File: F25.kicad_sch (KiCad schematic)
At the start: 37 parts, among them J3 B2B-PH-K-S, J4 USB_C_Receptacle_USB2.0_16P, Q1 IRLML6244, SW1 RESET, SW2 BOOT, U2 MPU-6050, U3 MS5611-01BA, U4 ESP32-S3-WROOM-1-N8, U5 AP2112K-3.3

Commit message: General Updates
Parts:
- U4: footprint ESP:ESP32-S3-WROOM-1_EXP -> RF_Module:ESP32-S3-WROOM-1
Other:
- note added: "I/O"
- note added: "MCU"
- note added: "MPU6050"
- note added: "MS5611"
- note added: "PULLUPS"
- title: Eggtimer Ion Flight Computer  -> MARS F25 Board
- moved on the sheet: C1, C10, C11, C2, C3, C4, C5, C6, C7, C8, CR1, D1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

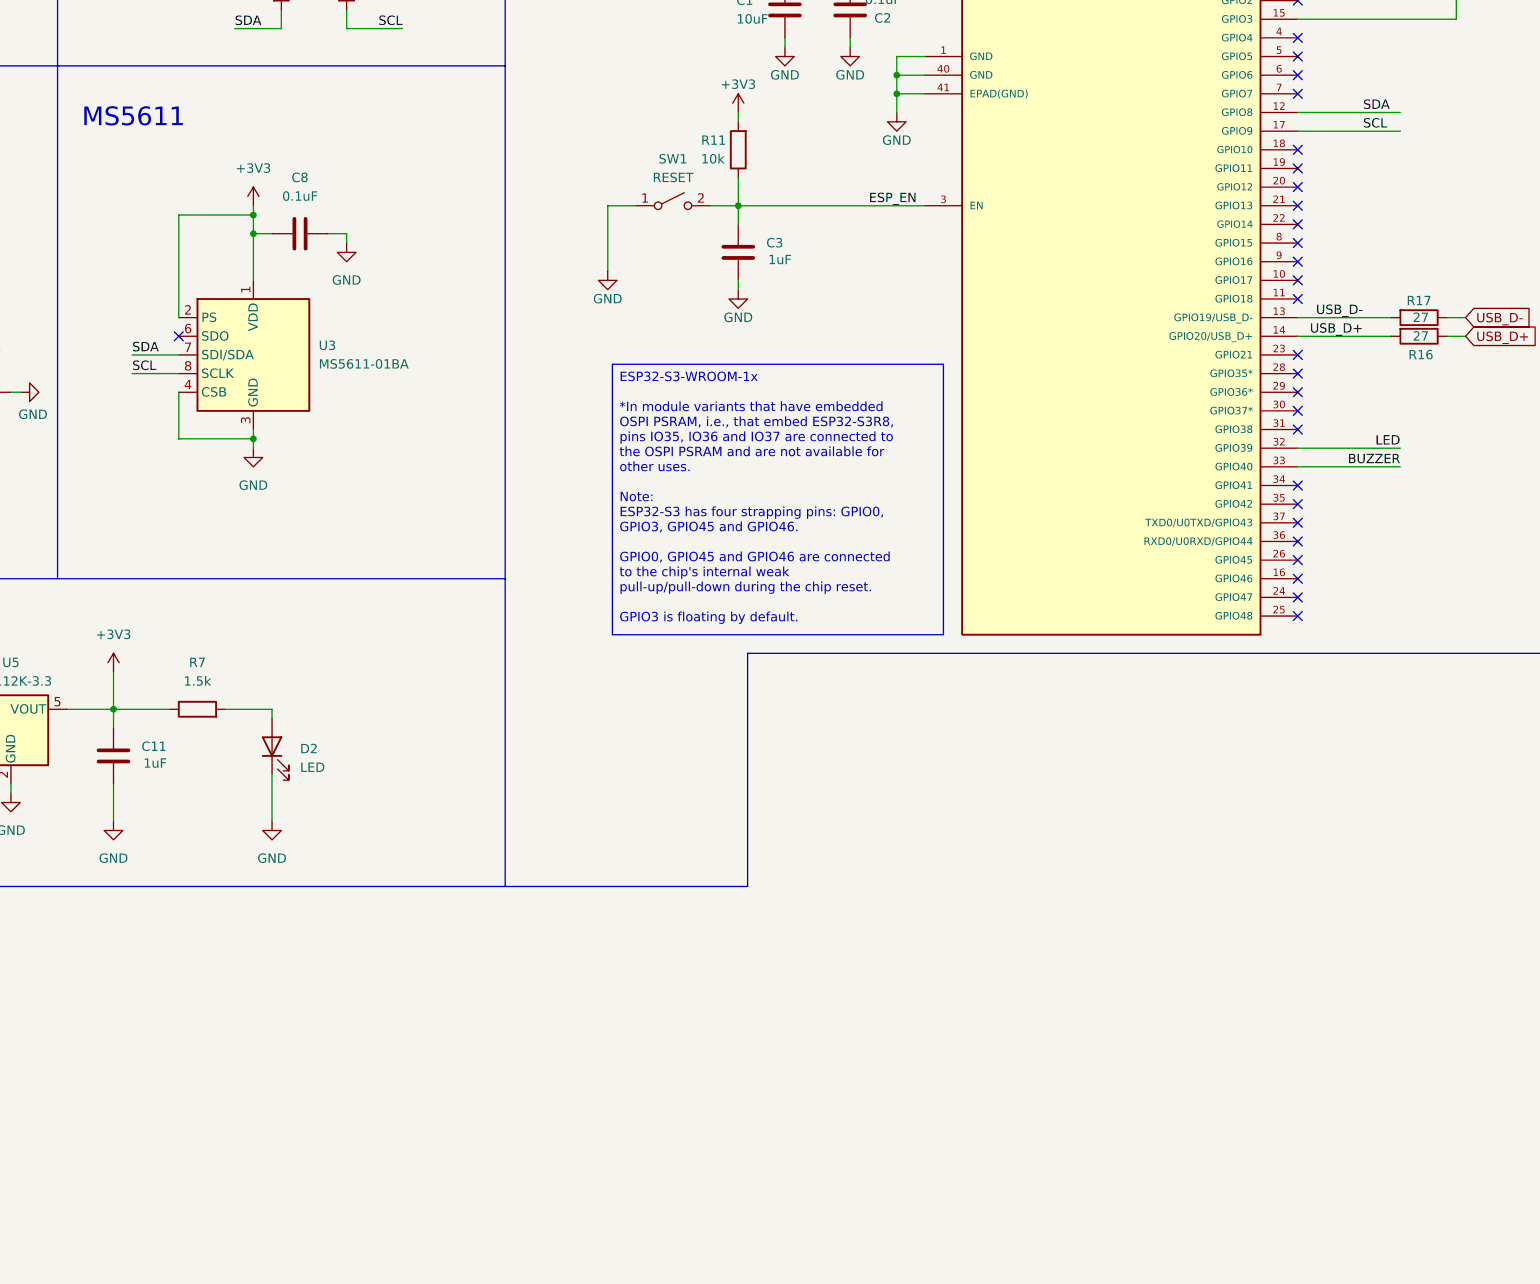
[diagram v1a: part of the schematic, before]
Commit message: MOVE TO SPI
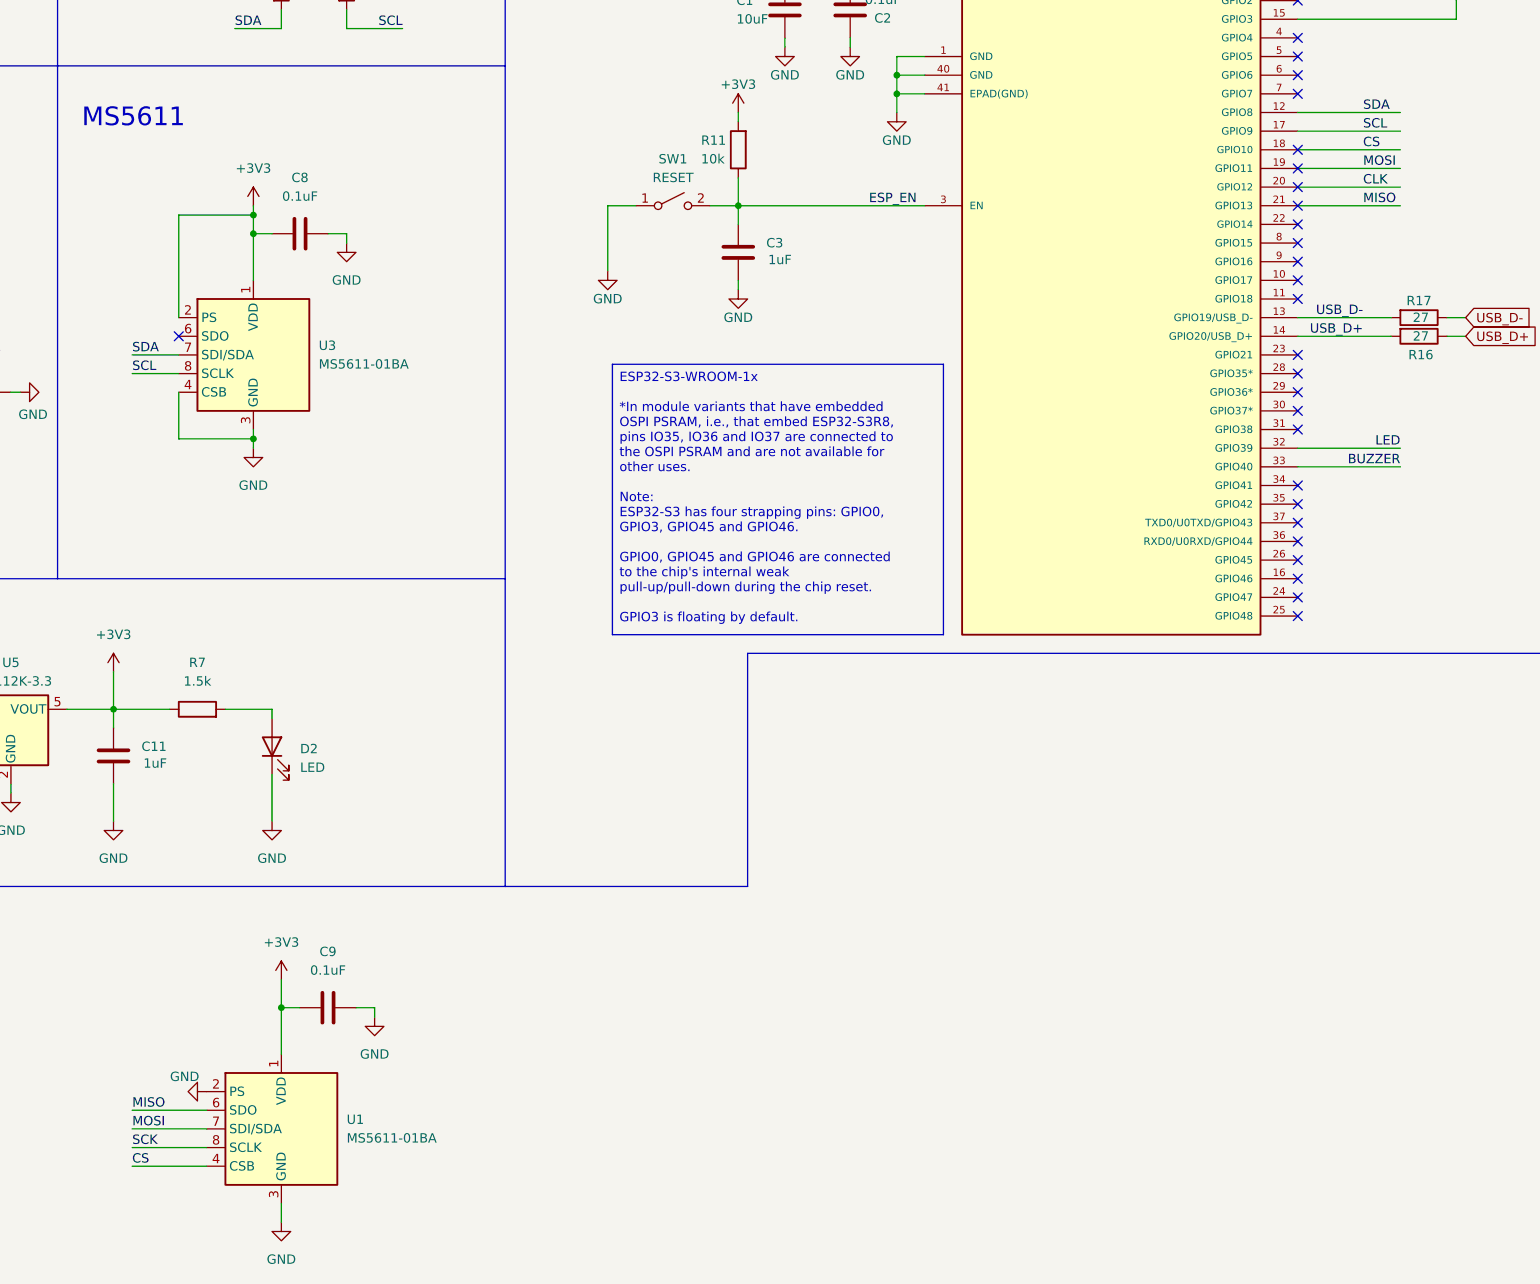
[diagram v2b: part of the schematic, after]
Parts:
- added C9: 0.1uF, Capacitor_SMD:C_0402_1005Metric, symbol Device:C
- added U1: MS5611-01BA, Package_LGA:LGA-8_3x5mm_P1.25mm, symbol Sensor_Pressure:MS5611-01BA
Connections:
- net +3V3: now also C9.1, U1.1 (VDD)
- net GND: now also C9.2, U1.2 (PS), U1.3 (GND)
- net CS: now reaches U4.18 (GPIO10)
- net CS: now also U1.4 (CSB), U1.5 (CSB)
- net MOSI: now reaches U4.19 (GPIO11)
- net MOSI: now also U1.7 (SDI/SDA)
- net CLK: now reaches U4.20 (GPIO12)
- net MISO: now reaches U4.21 (GPIO13)
- net MISO: now also U1.6 (SDO)
- new net SCK: U1.8 (SCLK)

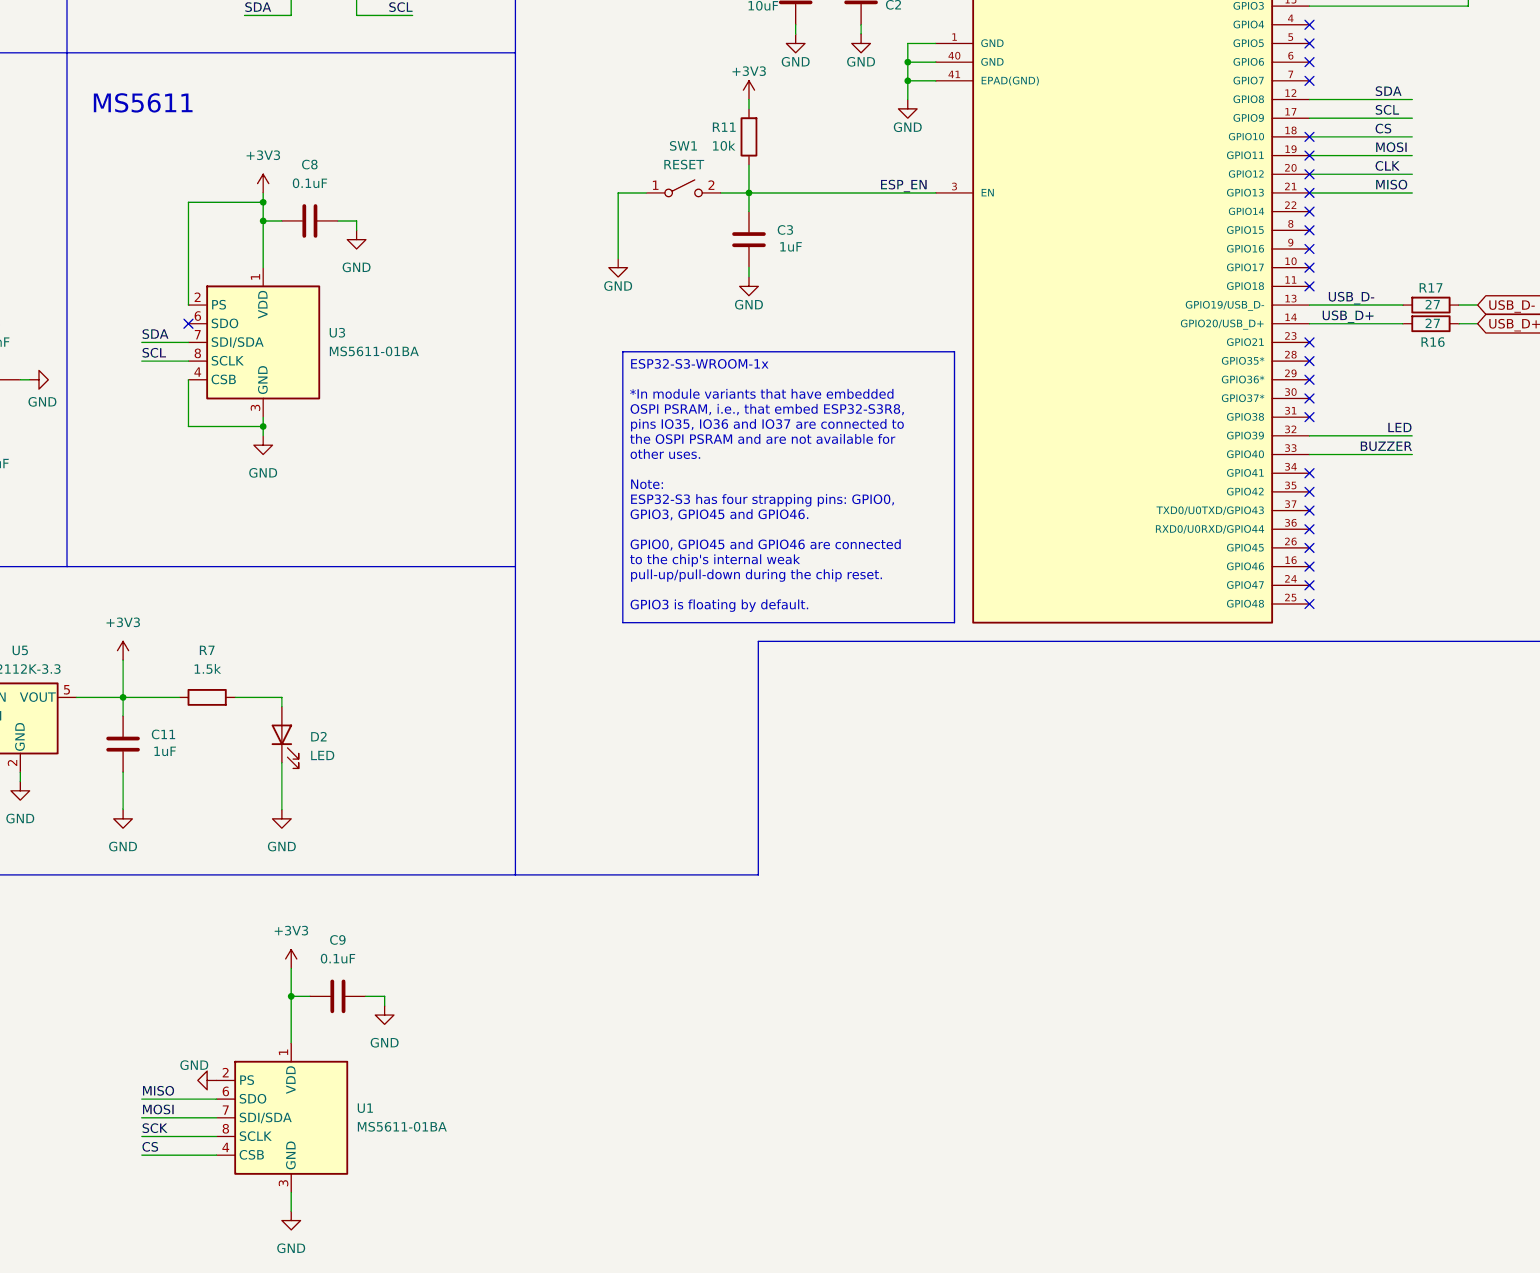
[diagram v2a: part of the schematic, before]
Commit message: Finish SPI MS6511
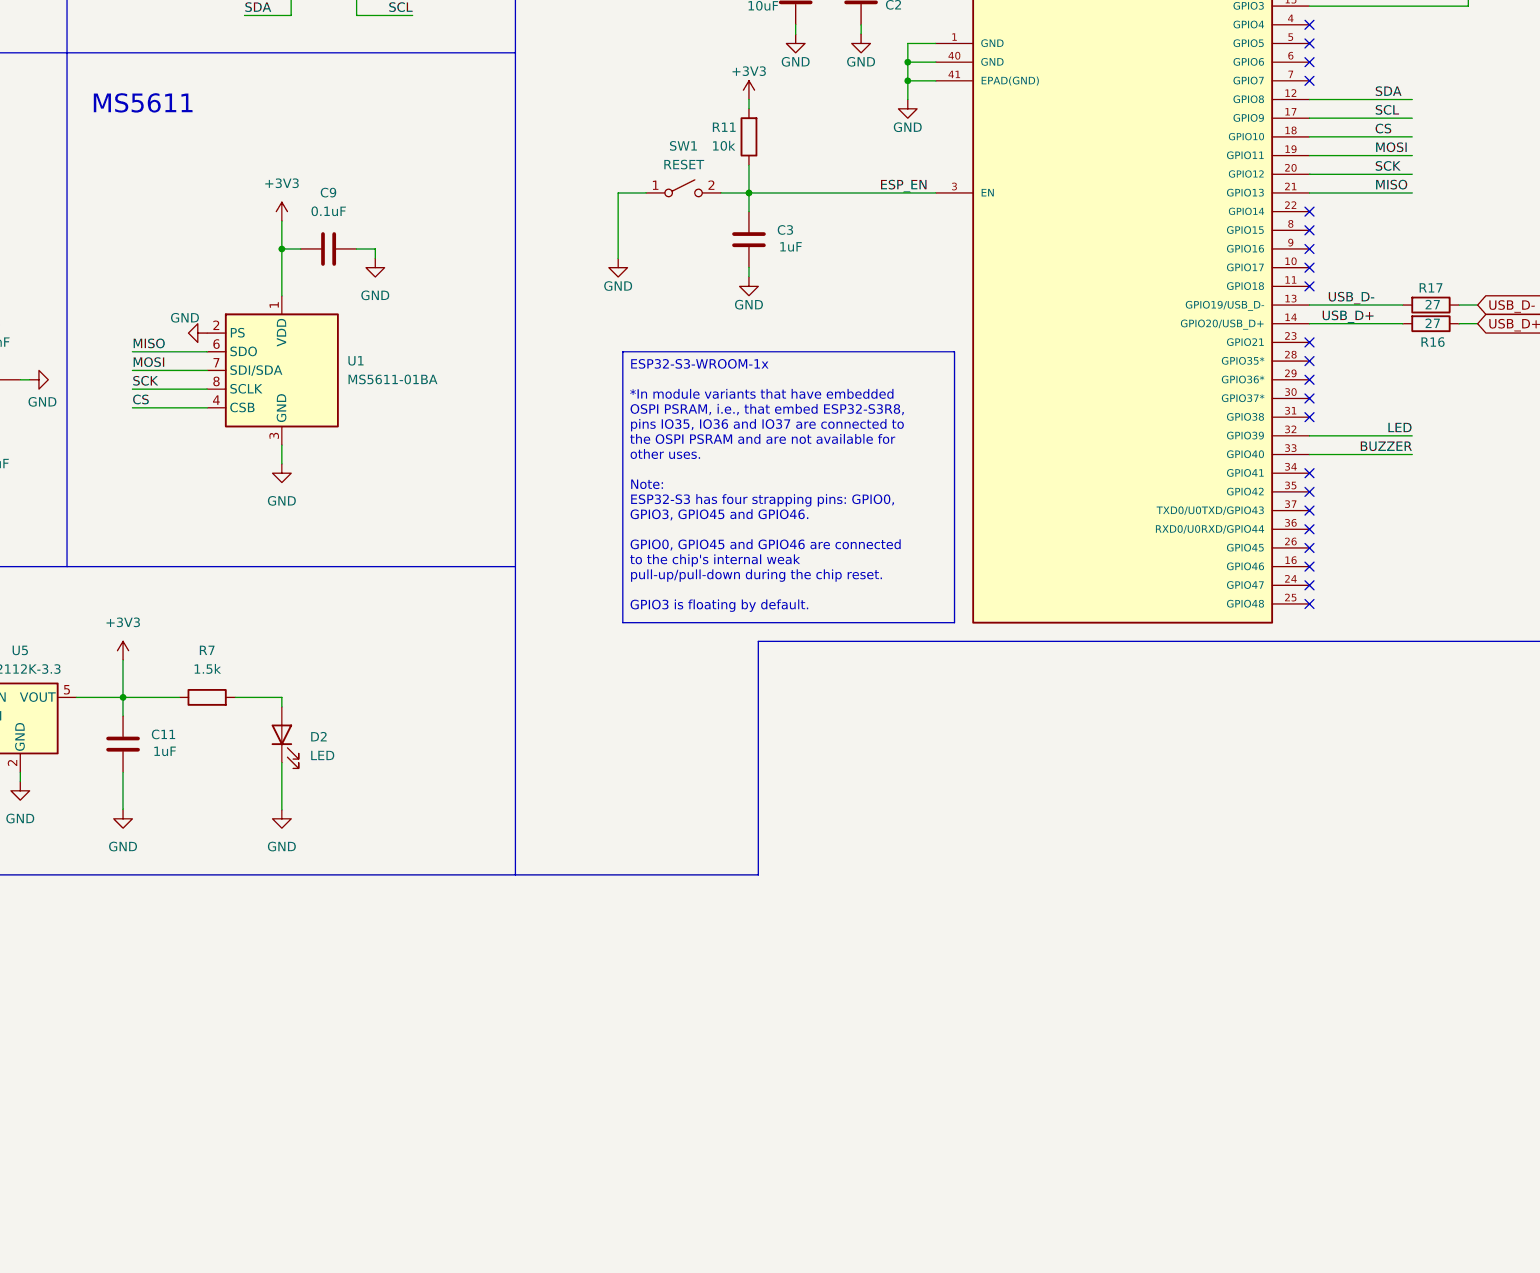
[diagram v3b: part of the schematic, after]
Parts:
- removed C8: 0.1uF, Capacitor_SMD:C_0402_1005Metric, symbol Device:C
- removed U3: MS5611-01BA, Package_LGA:LGA-8_3x5mm_P1.25mm, symbol Sensor_Pressure:MS5611-01BA
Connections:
- net CLK is gone; now on net SCK: U4.20 (GPIO12)
- no-connect marks 35 -> 30
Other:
- moved on the sheet: C9, U1

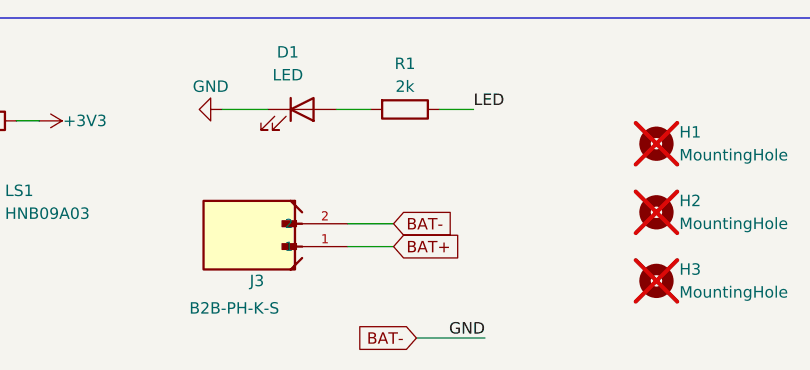
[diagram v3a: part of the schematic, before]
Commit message: Update LED Resistors
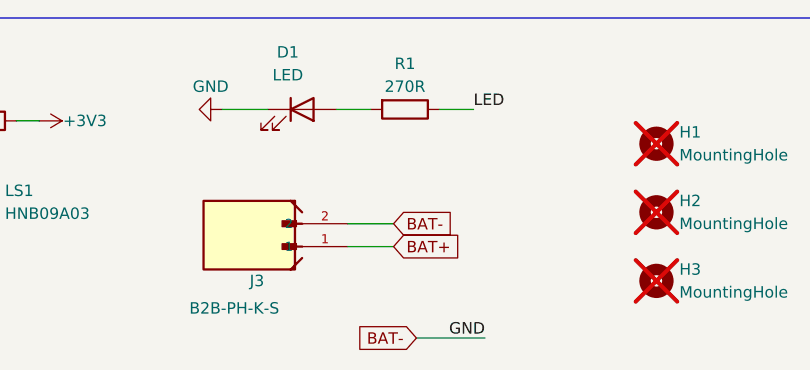
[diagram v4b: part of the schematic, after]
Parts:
- D1: LCSC C2290 -> C2288
- D2: LCSC C2286 -> C2290
- R1: value 2k -> 270R; LCSC C4109 -> C25099
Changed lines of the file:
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@@
 			)
 		)
-		(property "LCSC" "C2286"
+		(property "LCSC" "C2290"
 			(at 110.49 176.53 90)
 			(effects
@@
 			)
 		)
-		(property "LCSC" "C2290"
+		(property "LCSC" "C2288"
 			(at 218.44 24.13 0)
 			(effects
@@
 			)
 		)
-		(property "Value" "2k"
+		(property "Value" "270R"
 			(at 229.87 21.59 90)
 			(effects
@@
 			)
 		)
-		(property "LCSC" "C4109"
+		(property "LCSC" "C25099"
 			(at 229.87 24.13 0)
 			(effects
